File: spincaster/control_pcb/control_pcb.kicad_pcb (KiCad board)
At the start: 2 copper layers, 78.7 x 63.5 mm, 16 parts, among them J1 Extra, J2 Buzzer, J3 Relay, J4 Conn_01x05_Female, J5 Rocker, J6 PWR, SW2 IND_OFF, SW3 IND_ON, SW4 IND_PULSE, U1 LTV-817S, U2 LTV-817S, U3 LTV-817S

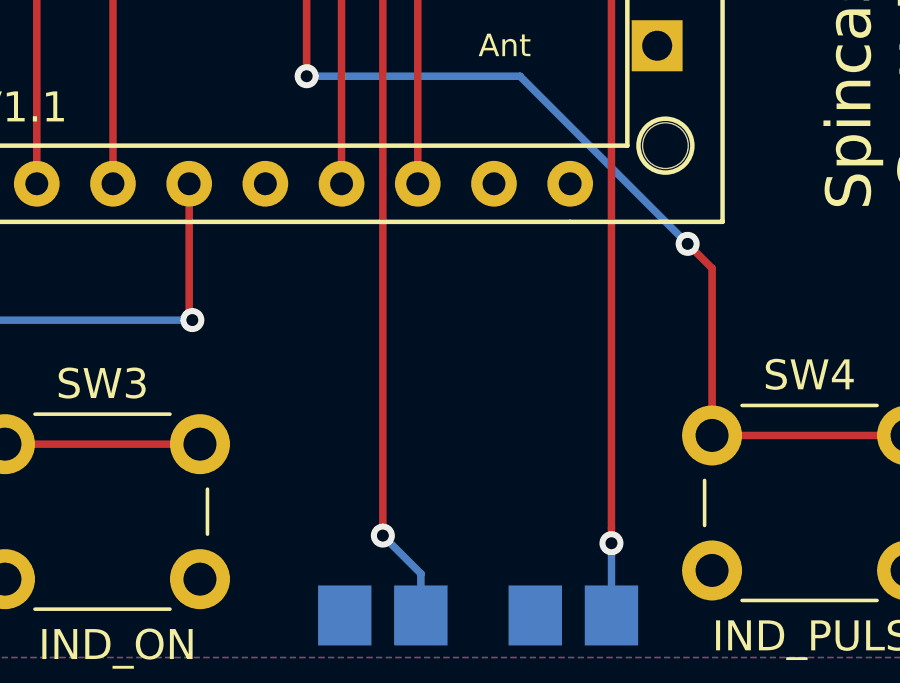
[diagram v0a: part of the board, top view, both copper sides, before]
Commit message: Add O2 sensor logic to firmware, check in control PCB kicad updates and o2 sensor mount ipynb
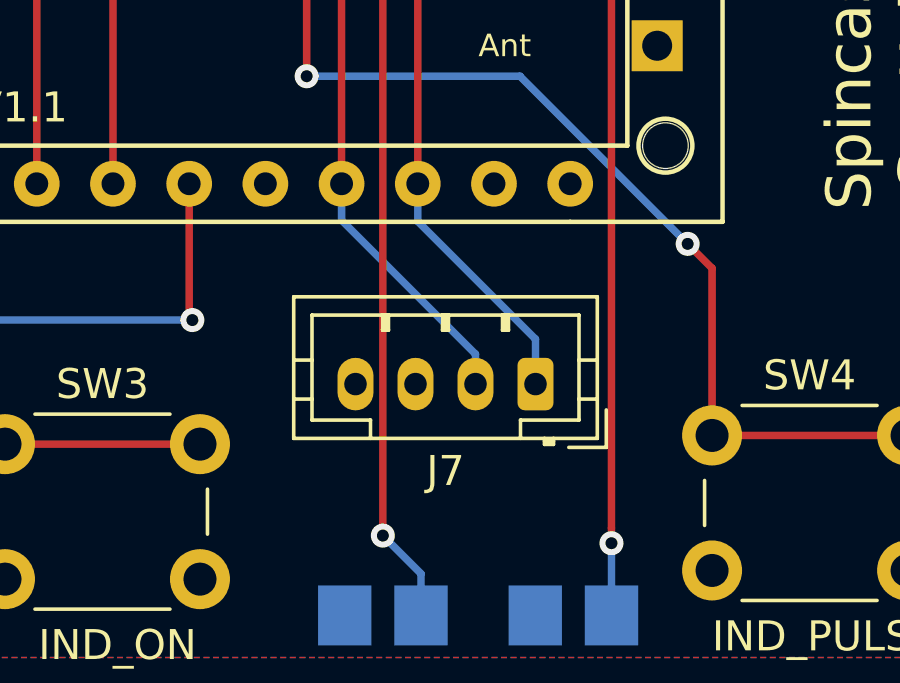
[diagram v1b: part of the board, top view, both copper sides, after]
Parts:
- added J7: Conn_01x04_Female, Connector_JST:JST_PH_B4B-PH-K_1x04_P2.00mm_Vertical, F.Cu at (158.2, 109.2)
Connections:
- TTGO1 pad 10: /GPIO37 -> /O2_RX
- TTGO1 pad 9: /GPIO38 -> /O2_TX
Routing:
- net /O2_TX: track 0.00 -> 26.0 mm, vias 0 -> 1
- net /O2_RX: track 0.00 -> 25.0 mm, vias 0 -> 1
- net /GPIO38: track 17.4 -> 0.00 mm, vias 1 -> 0
- net /GPIO37: track 16.7 -> 0.00 mm, vias 1 -> 0
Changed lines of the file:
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@@
   (net 26 "Net-(R2-Pad2)")
   (net 27 "/FET_OUT")
+  (net 28 "/O2_RX")
+  (net 29 "/O2_TX")
   (footprint "TTGO:TTGO_ESP32_TDisplay_v1.1" (layer "F.Cu")
     (at 114.956 103.842)
@@
       (net 15 "unconnected-(TTGO1-Pad8)") (pinfunction "SVN") (pintype "unspecified+no_connect"))
     (pad "9" thru_hole circle locked (at 36.83 -1.27) (size 1.524 1.524) (drill 0.762) (layers *.Cu *.Mask)
-      (net 1 "/GPIO38") (pinfunction "GPIO38") (pintype "unspecified"))
+      (net 29 "/O2_TX") (pinfunction "GPIO38") (pintype "unspecified"))
     (pad "10" thru_hole circle locked (at 39.37 -1.27) (size 1.524 1.524) (drill 0.762) (layers *.Cu *.Mask)
-      (net 2 "/GPIO37") (pinfunction "GPIO37") (pintype "unspecified"))
+      (net 28 "/O2_RX") (pinfunction "GPIO37") (pintype "unspecified"))
     (pad "11" thru_hole circle locked (at 41.91 -1.27) (size 1.524 1.524) (drill 0.762) (layers *.Cu *.Mask)
       (net 16 "unconnected-(TTGO1-Pad11)") (pinfunction "SVP") (pintype "unspecified+no_connect"))
@@
     (pad "24" thru_hole circle locked (at 16.51 -24.13) (size 1.524 1.524) (drill 0.762) (layers *.Cu *.Mask)
       (net 18 "unconnected-(TTGO1-Pad24)") (pinfunction "3.3V") (pintype "unspecified+no_connect"))
+  )
+  (footprint "Connector_JST:JST_PH_B4B-PH-K_1x04_P2.00mm_Vertical" (layer "F.Cu")
+    (at 158.25 109.25 180)
+    (descr "JST PH series connector, B4B-PH-K (http://www.jst-mfg.com/product/pdf/eng/ePH.pdf), generated with kicad-footprint-generator")
+    (tags "connector JST PH side entry")
+    (property "Sheetfile" "control_pcb.kicad_sch")
+    (property "Sheetname" "")
+    (attr through_hole)
+    (fp_text reference "J7" (at 3 -2.9) (layer "F.SilkS")
+      (effects (font (size 1 1) (thickness 0.15)))
+    )
+    (fp_text value "Conn_01x04_Female" (at 3 4) (layer "F.Fab")
+      (effects (font (size 1 1) (thickness 0.15)))
+    )
+    (fp_text user "${REFERENCE}" (at 3 1.5) (layer "F.Fab")
+      (effects (font (size 1 1) (thickness 0.15)))
+    )
+    (fp_line (start 8.06 -1.81) (end -2.06 -1.81) (layer "F.SilkS") (width 0.12))
+    (fp_line (start 0.5 -1.2) (end -1.45 -1.2) (layer "F.SilkS") (width 0.12))
+    (fp_line (start 1.1 1.8) (end 1.1 2.3) (layer "F.SilkS") (width 0.12))
+    (fp_line (start 8.06 0.8) (end 7.45 0.8) (layer "F.SilkS") (width 0.12))
+    (fp_line (start 3.1 1.8) (end 3.1 2.3) (layer "F.SilkS") (width 0.12))
+    (fp_line (start 4.9 1.8) (end 5.1 1.8) (layer "F.SilkS") (width 0.12))
+    (fp_line (start 8.06 2.91) (end 8.06 -1.81) (layer "F.SilkS") (width 0.12))
+    (fp_line (start -0.3 -2.01) (end -0.6 -2.01) (layer "F.SilkS") (width 0.12))
+    (fp_line (start 7.45 -1.2) (end 5.5 -1.2) (layer "F.SilkS") (width 0.12))
+    (fp_line (start -2.06 2.91) (end 8.06 2.91) (layer "F.SilkS") (width 0.12))
+    (fp_line (start -2.36 -2.11) (end -2.36 -0.86) (layer "F.SilkS") (width 0.12))
+    (fp_line (start 5 2.3) (end 5 1.8) (layer "F.SilkS") (width 0.12))
+    (fp_line (start 1 2.3) (end 1 1.8) (layer "F.SilkS") (width 0.12))
+    (fp_line (start -2.06 -1.81) (end -2.06 2.91) (layer "F.SilkS") (width 0.12))
+    (fp_line (start 0.5 -1.81) (end 0.5 -1.2) (layer "F.SilkS") (width 0.12))
+    (fp_line (start -2.06 0.8) (end -1.45 0.8) (layer "F.SilkS") (width 0.12))
+    (fp_line (start 8.06 -0.5) (end 7.45 -0.5) (layer "F.SilkS") (width 0.12))
+    (fp_line (start 2.9 1.8) (end 3.1 1.8) (layer "F.SilkS") (width 0.12))
+    (fp_line (start -0.3 -1.91) (end -0.6 -1.91) (layer "F.SilkS") (width 0.12))
+    (fp_line (start 4.9 2.3) (end 4.9 1.8) (layer "F.SilkS") (width 0.12))
+    (fp_line (start 0.9 1.8) (end 1.1 1.8) (layer "F.SilkS") (width 0.12))
+    (fp_line (start 0.9 2.3) (end 0.9 1.8) (layer "F.SilkS") (width 0.12))
+    (fp_line (start 3 2.3) (end 3 1.8) (layer "F.SilkS") (width 0.12))
+    (fp_line (start -0.3 -1.81) (end -0.3 -2.01) (layer "F.SilkS") (width 0.12))
+    (fp_line (start 2.9 2.3) (end 2.9 1.8) (layer "F.SilkS") (width 0.12))
+    (fp_line (start -2.06 -0.5) (end -1.45 -0.5) (layer "F.SilkS") (width 0.12))
+    (fp_line (start -0.6 -2.01) (end -0.6 -1.81) (layer "F.SilkS") (width 0.12))
+    (fp_line (start 7.45 2.3) (end 7.45 -1.2) (layer "F.SilkS") (width 0.12))
+    (fp_line (start -1.45 -1.2) (end -1.45 2.3) (layer "F.SilkS") (width 0.12))
+    (fp_line (start 5.1 1.8) (end 5.1 2.3) (layer "F.SilkS") (width 0.12))
+    (fp_line (start -1.11 -2.11) (end -2.36 -2.11) (layer "F.SilkS") (width 0.12))
+    (fp_line (start -1.45 2.3) (end 7.45 2.3) (layer "F.SilkS") (width 0.12))
+    (fp_line (start 5.5 -1.2) (end 5.5 -1.81) (layer "F.SilkS") (width 0.12))
+    (fp_line (start -2.45 3.3) (end 8.45 3.3) (layer "F.CrtYd") (width 0.05))
+    (fp_line (start -2.45 -2.2) (end -2.45 3.3) (layer "F.CrtYd") (width 0.05))
+    (fp_line (start 8.45 -2.2) (end -2.45 -2.2) (layer "F.CrtYd") (width 0.05))
+    (fp_line (start 8.45 3.3) (end 8.45 -2.2) (layer "F.CrtYd") (width 0.05))
+    (fp_line (start -1.95 2.8) (end 7.95 2.8) (layer "F.Fab") (width 0.1))
+    (fp_line (start -1.95 -1.7) (end -1.95 2.8) (layer "F.Fab") (width 0.1))
+    (fp_line (start -2.36 -2.11) (end -2.36 -0.86) (layer "F.Fab") (width 0.1))
+    (fp_line (start -1.11 -2.11) (end -2.36 -2.11) (layer "F.Fab") (width 0.1))
+    (fp_line (start 7.95 2.8) (end 7.95 -1.7) (layer "F.Fab") (width 0.1))
+    (fp_line (start 7.95 -1.7) (end -1.95 -1.7) (layer "F.Fab") (width 0.1))
+    (pad "1" thru_hole roundrect (at 0 0 180) (size 1.2 1.75) (drill 0.75) (layers *.Cu *.Mask) (roundrect_rratio 0.208333)
+      (net 28 "/O2_RX") (pinfunction "Pin_1") (pintype "passive"))
+    (pad "2" thru_hole oval (at 2 0 180) (size 1.2 1.75) (drill 0.75) (layers *.Cu *.Mask)
+      (net 29 "/O2_TX") (pinfunction "Pin_2") (pintype "passive"))
+    (pad "3" thru_hole oval (at 4 0 180) (size 1.2 1.75) (drill 0.75) (layers *.Cu *.Mask)
+      (net 19 "VDD") (pinfunction "Pin_3") (pintype "passive"))
+    (pad "4" thru_hole oval (at 6 0 180) (size 1.2 1.75) (drill 0.75) (layers *.Cu *.Mask)
+      (net 20 "GNDD") (pinfunction "Pin_4") (pintype "passive"))
+    (model "${KICAD6_3DMODEL_DIR}/Connector_JST.3dshapes/JST_PH_B4B-PH-K_1x04_P2.00mm_Vertical.wrl"
+      (offset (xyz 0 0 0))
+      (scale (xyz 1 1 1))
+      (rotate (xyz 0 0 0))
+    )
   )
   (footprint "Button_Switch_THT:SW_PUSH_6mm_H5mm" (layer "F.Cu")
@@
     (effects (font (size 1.5 1.5) (thickness 0.3)))
   )
-  (segment (start 151.786 102.572) (end 151.786 95.792) (width 0.25) (layer "F.Cu") (net 1))
-  (segment (start 151.786 95.792) (end 151.892 95.686) (width 0.25) (layer "F.Cu") (net 1))
-  (via (at 151.892 95.686) (size 0.8) (drill 0.4) (layers "F.Cu" "B.Cu") (net 1))
-  (segment (start 151.892 95.686) (end 152.146 95.432) (width 0.25) (layer "B.Cu") (net 1))
-  (segment (start 152.146 95.432) (end 162.306 95.432) (width 0.25) (layer "B.Cu") (net 1))
-  (segment (start 154.326 94.522) (end 154.326 102.572) (width 0.25) (layer "F.Cu") (net 2))
-  (segment (start 154.432 94.416) (end 154.326 94.522) (width 0.25) (layer "F.Cu") (net 2))
-  (via (at 154.432 94.416) (size 0.8) (drill 0.4) (layers "F.Cu" "B.Cu") (net 2))
-  (segment (start 160.782 94.416) (end 154.432 94.416) (width 0.25) (layer "B.Cu") (net 2))
-  (segment (start 162.306 92.892) (end 160.782 94.416) (width 0.25) (layer "B.Cu") (net 2))
   (segment (start 143.002 81.088) (end 143.002 81.97) (width 0.25) (layer "F.Cu") (net 3))
   (segment (start 160.02 88.066) (end 162.306 90.352) (width 0.25) (layer "F.Cu") (net 3))
@@
   (segment (start 139.7 108.204) (end 139.954 108.204) (width 0.25) (layer "B.Cu") (net 27))
   (segment (start 129.286 111.76) (end 136.144 111.76) (width 0.25) (layer "B.Cu") (net 27))
+  (segment (start 154.326 94.522) (end 154.326 102.572) (width 0.25) (layer "F.Cu") (net 28))
+  (segment (start 154.432 94.416) (end 154.326 94.522) (width 0.25) (layer "F.Cu") (net 28))
+  (via (at 154.432 94.416) (size 0.8) (drill 0.4) (layers "F.Cu" "B.Cu") (net 28))
+  (segment (start 154.326 103.826) (end 158.25 107.75) (width 0.25) (layer "B.Cu") (net 28))
+  (segment (start 160.782 94.416) (end 154.432 94.416) (width 0.25) (layer "B.Cu") (net 28))
+  (segment (start 162.306 92.892) (end 160.782 94.416) (width 0.25) (layer "B.Cu") (net 28))
+  (segment (start 158.25 107.75) (end 158.25 109.25) (width 0.25) (layer "B.Cu") (net 28))
+  (segment (start 154.326 102.572) (end 154.326 103.826) (width 0.25) (layer "B.Cu") (net 28))
+  (segment (start 151.786 102.572) (end 151.786 95.792) (width 0.25) (layer "F.Cu") (net 29))
+  (segment (start 151.786 95.792) (end 151.892 95.686) (width 0.25) (layer "F.Cu") (net 29))
+  (via (at 151.892 95.686) (size 0.8) (drill 0.4) (layers "F.Cu" "B.Cu") (net 29))
+  (segment (start 156.25 108.25) (end 156.25 109.25) (width 0.25) (layer "B.Cu") (net 29))
+  (segment (start 151.786 103.786) (end 156.25 108.25) (width 0.25) (layer "B.Cu") (net 29))
+  (segment (start 151.786 102.572) (end 151.786 103.786) (width 0.25) (layer "B.Cu") (net 29))
+  (segment (start 151.892 95.686) (end 152.146 95.432) (width 0.25) (layer "B.Cu") (net 29))
+  (segment (start 152.146 95.432) (end 162.306 95.432) (width 0.25) (layer "B.Cu") (net 29))
   (zone (net 19) (net_name "VDD") (layer "F.Cu") (hatch edge 0.508)
     (connect_pads (clearance 0.508))
